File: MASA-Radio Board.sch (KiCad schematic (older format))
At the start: 50 parts, among them IC1 FAN4010IL6X_F113, IC2 FAN4010IL6X_F113, J1 Conn_01x02, J2 Conn_01x02_Male, J3 Conn_01x02_Male, J4 Conn_01x03_Male, J5 Conn_01x06, J6 SC_19-20, J7 Conn_01x06, J8 Conn_01x02, J9 UJ2-MBH-1-SMT-TR, U1 MP5077GG-Z, U2 BL654PA, U3 MIC5504-3.3YM5, U4 MP5077GG-Z

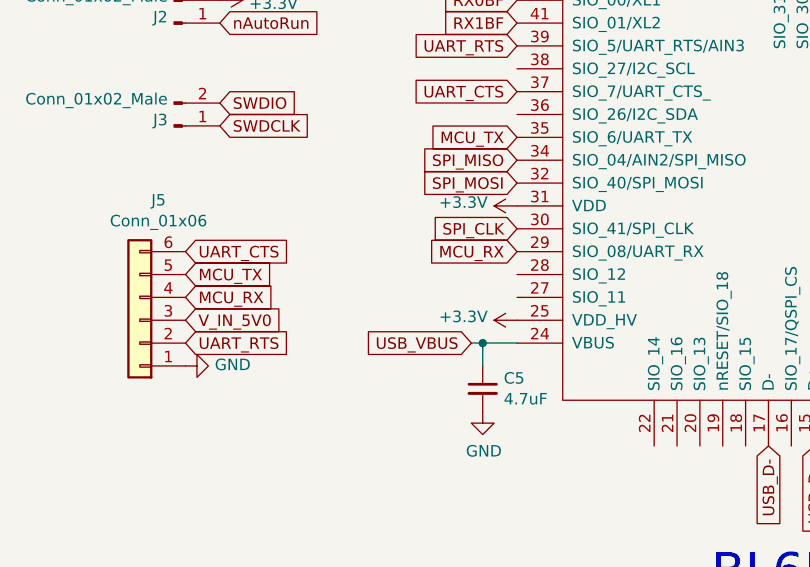
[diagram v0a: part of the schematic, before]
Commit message: Added caps on 3.3V MCU
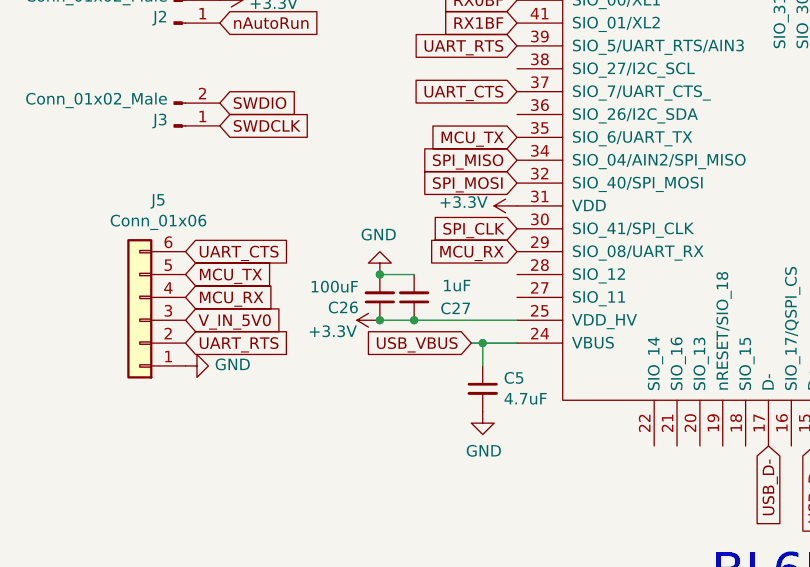
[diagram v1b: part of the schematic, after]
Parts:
- added C26: 100uF, Capacitor_SMD:C_0603_1608Metric, symbol Device:C_Small
- added C27: 1uF, Capacitor_SMD:C_0603_1608Metric, symbol Device:C_Small
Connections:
- wire segments 94 -> 97
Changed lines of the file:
@@
 L power:+3.3V #PWR010
 U 1 1 5E17DA05
-P 11450 4400
-F 0 "#PWR010" H 11450 4250 50  0001 C CNN
-F 1 "+3.3V" V 11465 4528 50  0000 L CNN
-F 2 "" H 11450 4400 50  0001 C CNN
-F 3 "" H 11450 4400 50  0001 C CNN
-	1    11450 4400
+P 10850 4400
+F 0 "#PWR010" H 10850 4250 50  0001 C CNN
+F 1 "+3.3V" V 10800 4500 50  0000 L CNN
+F 2 "" H 10850 4400 50  0001 C CNN
+F 3 "" H 10850 4400 50  0001 C CNN
+	1    10850 4400
 	0    -1   -1   0
 $EndComp
@@
 Text GLabel 11250 4500 0    50   Input ~ 0
 USB_VBUS
-$Comp
-L power:GND #PWR014
-U 1 1 5E19D471
-P 11300 4800
-F 0 "#PWR014" H 11300 4550 50  0001 C CNN
-F 1 "GND" H 11305 4627 50  0000 C CNN
-F 2 "" H 11300 4800 50  0001 C CNN
-F 3 "" H 11300 4800 50  0001 C CNN
-	1    11300 4800
-	1    0    0    -1
-$EndComp
-$Comp
-L Device:C_Small C5
-U 1 1 5E19C8DE
-P 11300 4700
-F 0 "C5" H 11392 4746 50  0000 L CNN
-F 1 "4.7uF" H 11392 4655 50  0000 L CNN
-F 2 "Capacitor_SMD:C_0603_1608Metric" H 11300 4700 50  0001 C CNN
-F 3 "~" H 11300 4700 50  0001 C CNN
-	1    11300 4700
-	1    0    0    -1
-$EndComp
 Connection ~ 11300 4500
 Text GLabel 11850 8400 0    50   Input ~ 0
@@
 	1    0    0    1
 $EndComp
-$Comp
-L MASA_Library:BL654PA U2
-U 1 1 5E18798E
-P 13150 3750
-F 0 "U2" H 14894 3796 50  0000 L CNN
-F 1 "BL654PA" H 14894 3705 50  0000 L CNN
-F 2 "MASA_Library:BL654PA" H 13150 3750 50  0001 C CNN
-F 3 "" H 13150 3750 50  0001 C CNN
-	1    13150 3750
-	1    0    0    -1
-$EndComp
 Text Notes 12300 13000 0    157  ~ 0
 Temperature Sensor
-Wire Wire Line
-	11300 4500 11450 4500
 Text Notes 15500 2850 0    50   ~ 0
 Reserve I/O Pins for:
@@
 Text GLabel 12900 2550 1    50   Input ~ 0
 TSENSE
+Wire Wire Line
+	11300 4500 11450 4500
+$Comp
+L MASA_Library:BL654PA U2
+U 1 1 5E18798E
+P 13150 3750
+F 0 "U2" H 14894 3796 50  0000 L CNN
+F 1 "BL654PA" H 14894 3705 50  0000 L CNN
+F 2 "MASA_Library:BL654PA" H 13150 3750 50  0001 C CNN
+F 3 "" H 13150 3750 50  0001 C CNN
+	1    13150 3750
+	1    0    0    -1
+$EndComp
+$Comp
+L Device:C_Small C5
+U 1 1 5E19C8DE
+P 11300 4700
+F 0 "C5" H 11392 4746 50  0000 L CNN
+F 1 "4.7uF" H 11392 4655 50  0000 L CNN
+F 2 "Capacitor_SMD:C_0603_1608Metric" H 11300 4700 50  0001 C CNN
+F 3 "~" H 11300 4700 50  0001 C CNN
+	1    11300 4700
+	1    0    0    -1
+$EndComp
+$Comp
+L power:GND #PWR014
+U 1 1 5E19D471
+P 11300 4800
+F 0 "#PWR014" H 11300 4550 50  0001 C CNN
+F 1 "GND" H 11305 4627 50  0000 C CNN
+F 2 "" H 11300 4800 50  0001 C CNN
+F 3 "" H 11300 4800 50  0001 C CNN
+	1    11300 4800
+	1    0    0    -1
+$EndComp
+$Comp
+L Device:C_Small C27
+U 1 1 5E84D23C
+P 11000 4300
+F 0 "C27" H 10750 4350 50  0000 L CNN
+F 1 "1uF" H 10750 4250 50  0000 L CNN
+F 2 "Capacitor_SMD:C_0603_1608Metric" H 11000 4300 50  0001 C CNN
+F 3 "~" H 11000 4300 50  0001 C CNN
+	1    11000 4300
+	-1   0    0    1
+$EndComp
+$Comp
+L Device:C_Small C26
+U 1 1 5E84FF5A
+P 10850 4300
+F 0 "C26" H 10942 4346 50  0000 L CNN
+F 1 "100uF" H 10942 4255 50  0000 L CNN
+F 2 "Capacitor_SMD:C_0603_1608Metric" H 10850 4300 50  0001 C CNN
+F 3 "~" H 10850 4300 50  0001 C CNN
+	1    10850 4300
+	-1   0    0    1
+$EndComp
+$Comp
+L power:GND #PWR073
+U 1 1 5E84FF60
+P 10850 4200
+F 0 "#PWR073" H 10850 3950 50  0001 C CNN
+F 1 "GND" H 10855 4027 50  0000 C CNN
+F 2 "" H 10850 4200 50  0001 C CNN
+F 3 "" H 10850 4200 50  0001 C CNN
+	1    10850 4200
+	-1   0    0    1
+$EndComp
+Connection ~ 10850 4200
+Wire Wire Line
+	11000 4400 10850 4400
+Connection ~ 10850 4400
+Wire Wire Line
+	11000 4400 11450 4400
+Connection ~ 11000 4400
+Wire Wire Line
+	11000 4200 10850 4200
 $EndSCHEMATC

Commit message: Fixed caps and added grounding
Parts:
- C26: value 100uF -> 100nF
- C27: value 1uF -> 1nF
- MOD1: symbol dk_RF-Transceiver-Modules:XBP9B-DPST-001 -> MASA-Radio-Board-rescue:XBP9B-DPST-001-dk_RF-Transceiver-Modules
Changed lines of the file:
@@
 EESchema Schematic File Version 4
+LIBS:MASA-Radio Board-cache
 EELAYER 30 0
 EELAYER END
@@
 	4850 7650 4950 7650
 $Comp
-L dk_RF-Transceiver-Modules:XBP9B-DPST-001 MOD1
+L MASA-Radio-Board-rescue:XBP9B-DPST-001-dk_RF-Transceiver-Modules MOD1
 U 1 1 5E2D5997
 P 4950 8600
@@
 P 11000 4300
 F 0 "C27" H 10750 4350 50  0000 L CNN
-F 1 "1uF" H 10750 4250 50  0000 L CNN
+F 1 "1nF" H 10750 4250 50  0000 L CNN
 F 2 "Capacitor_SMD:C_0603_1608Metric" H 11000 4300 50  0001 C CNN
 F 3 "~" H 11000 4300 50  0001 C CNN
@@
 P 10850 4300
 F 0 "C26" H 10942 4346 50  0000 L CNN
-F 1 "100uF" H 10942 4255 50  0000 L CNN
+F 1 "100nF" H 10942 4255 50  0000 L CNN
 F 2 "Capacitor_SMD:C_0603_1608Metric" H 10850 4300 50  0001 C CNN
 F 3 "~" H 10850 4300 50  0001 C CNN

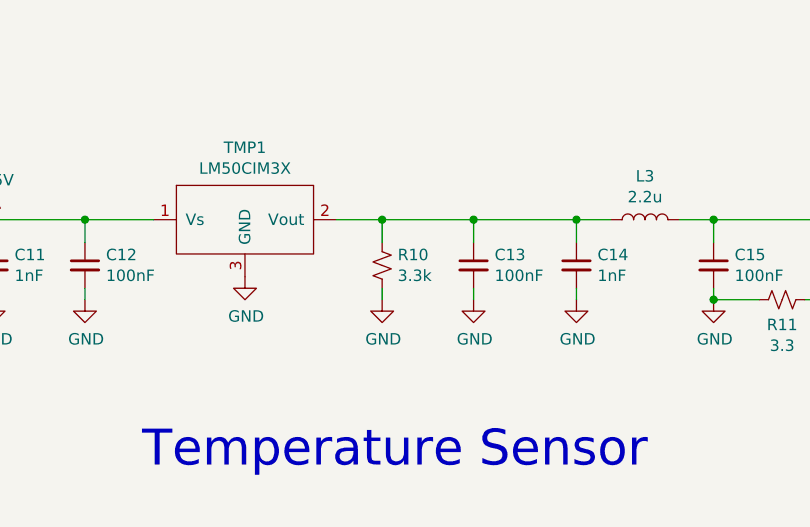
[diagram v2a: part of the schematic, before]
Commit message: Removed resistor from temp sensor
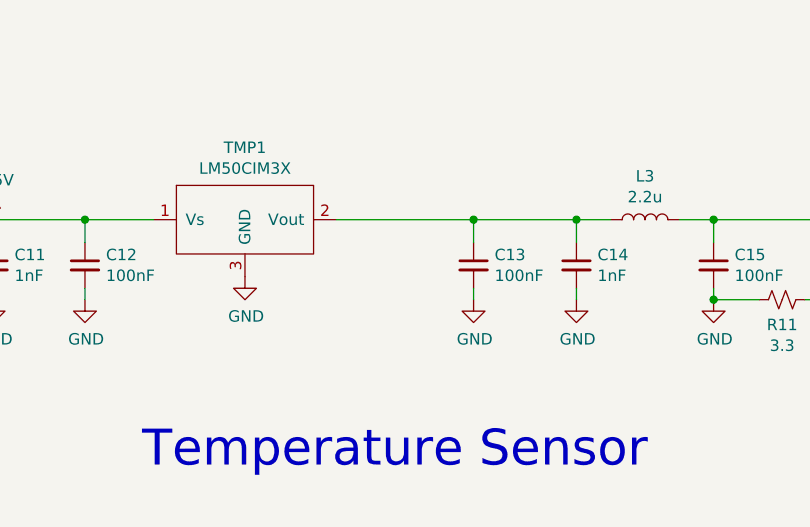
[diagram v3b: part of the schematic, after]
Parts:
- removed R10: 3.3k, Resistor_SMD:R_0603_1608Metric, symbol Device:R_Small_US
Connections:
- wire segments 97 -> 94
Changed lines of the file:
@@
 EELAYER 30 0
 EELAYER END
-$Descr A1 33110 23386
+$Descr A2 23386 16535
 encoding utf-8
 Sheet 1 2
@@
 	13750 11900 14200 11900
 Connection ~ 13750 11900
-Connection ~ 13350 11900
-Wire Wire Line
-	13350 11900 13750 11900
 Wire Wire Line
 	13750 12250 13750 12200
@@
 F 3 "~" H 13750 12100 50  0001 C CNN
 	1    13750 12100
-	1    0    0    -1
-$EndComp
-Wire Wire Line
-	13350 11900 13150 11900
-Wire Wire Line
-	13350 12000 13350 11900
-Wire Wire Line
-	13350 12250 13350 12200
-$Comp
-L power:GND #PWR043
-U 1 1 5E22C0FA
-P 13350 12250
-F 0 "#PWR043" H 13350 12000 50  0001 C CNN
-F 1 "GND" H 13355 12077 50  0000 C CNN
-F 2 "" H 13350 12250 50  0001 C CNN
-F 3 "" H 13350 12250 50  0001 C CNN
-	1    13350 12250
-	1    0    0    -1
-$EndComp
-$Comp
-L Device:R_Small_US R10
-U 1 1 5E22780B
-P 13350 12100
-F 0 "R10" H 13418 12146 50  0000 L CNN
-F 1 "3.3k" H 13418 12055 50  0000 L CNN
-F 2 "Resistor_SMD:R_0603_1608Metric" H 13350 12100 50  0001 C CNN
-F 3 "~" H 13350 12100 50  0001 C CNN
-	1    13350 12100
 	1    0    0    -1
 $EndComp
@@
 Wire Wire Line
 	11000 4200 10850 4200
+Wire Wire Line
+	13150 11900 13750 11900
 $EndSCHEMATC

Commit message: Added filters and connected missing analog lines. Also fixed USB
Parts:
- removed C1, C9: 10nF, Capacitor_SMD:C_0402_1005Metric, symbol Device:C_Small
- removed C10: 22nF, Capacitor_SMD:C_0603_1608Metric, symbol Device:C_Small
- removed C11, C14, C27: 1nF, Capacitor_SMD:C_0603_1608Metric, symbol Device:C_Small
- removed C12, C13, C15, C26: 100nF, Capacitor_SMD:C_0603_1608Metric, symbol Device:C_Small
- removed C16: 2.2uF, Capacitor_SMD:C_0603_1608Metric, symbol Device:C_Small
- removed C17, C4, C6, C8: 1uF, Capacitor_SMD:C_0603_1608Metric, symbol Device:C_Small
- removed C2: 22uF, Capacitor_SMD:C_0603_1608Metric, symbol Device:C_Small
- removed C3: 0.68uF, Capacitor_SMD:C_0603_1608Metric, symbol Device:C_Small
- removed C5: 4.7uF, Capacitor_SMD:C_0603_1608Metric, symbol Device:C_Small
- removed C7: 47pF, Capacitor_SMD:C_0603_1608Metric, symbol Device:C_Small
- removed D1, D2: D_TVS, Diode_SMD:D_SOD-523, symbol Device:D_TVS
- removed IC1, IC2: FAN4010IL6X_F113, MASA_Library:6-LEAD_MICROPAK, symbol FAN4010IL6X_F113:FAN4010IL6X_F113
- removed J1, J8: Conn_01x02, Jumper:SolderJumper-2_P1.3mm_Open_TrianglePad1.0x1.5mm, symbol Connector_Generic:Conn_01x02
- removed J2, J3: Conn_01x02_Male, Connector_PinHeader_2.54mm:PinHeader_1x02_P2.54mm_Vertical, symbol Connector:Conn_01x02_Male
- removed J4: Conn_01x03_Male, Connector_PinHeader_2.54mm:PinHeader_1x03_P2.54mm_Vertical, symbol Connector:Conn_01x03_Male
- removed J5, J7: Conn_01x06, Connector_PinHeader_2.54mm:PinHeader_1x06_P2.54mm_Vertical, symbol Connector_Generic:Conn_01x06
- removed J6: SC_19-20, MASA_Library:Stack_Connector_2019_2020, symbol MASA_Library:SC_19-20
- removed J9: UJ2-MBH-1-SMT-TR, digikey-footprints:USB_Mini_B_Female_UJ2-MBH-1-SMT-TR, symbol MASA-Radio-Board-rescue:UJ2-MBH-1-SMT-TR-dk_USB-DVI-HDMI-Connectors
- removed L1, L2: 4.7uH, Inductor_SMD:L_0603_1608Metric, symbol Device:L
- removed L3: 2.2u, Inductor_SMD:L_0603_1608Metric, symbol Device:L
- removed MOD1: XBP9B-DPST-001, digikey-footprints:XBEE_PRO-20_THT, symbol MASA-Radio-Board-rescue:XBP9B-DPST-001-dk_RF-Transceiver-Modules
- removed R1: 1, Resistor_SMD:R_0603_1608Metric, symbol Device:R_US
- removed R11: 3.3, Resistor_SMD:R_0603_1608Metric, symbol Device:R_Small_US
- removed R2: 200k, Resistor_SMD:R_0603_1608Metric, symbol Device:R_US
- removed R3: 200m, Resistor_SMD:R_0603_1608Metric, symbol Device:R_US
- removed R4: 3k, Resistor_SMD:R_0603_1608Metric, symbol Device:R_US
- removed R5: 100k, Resistor_SMD:R_0603_1608Metric, symbol Device:R_Small_US
- removed R6: 1, Resistor_SMD:R_0402_1005Metric, symbol Device:R_US
- removed R7: 1, Resistor_SMD:R_0603_1608Metric, symbol Device:R_Small_US
- removed R8: 3k, Resistor_SMD:R_0603_1608Metric, symbol Device:R_Small_US
- removed R9: 820k, Resistor_SMD:R_0603_1608Metric, symbol Device:R_Small_US
- removed TMP1: LM50CIM3X, Package_TO_SOT_SMD:SOT-23, symbol MASA_Library:LM50CIM3X
- removed U1, U4: MP5077GG-Z, MASA_Library:MP5077GG-Z, symbol MASA_Library:MP5077GG-Z
- removed U2: BL654PA, MASA_Library:BL654PA, symbol MASA_Library:BL654PA
- removed U3: MIC5504-3.3YM5, Package_TO_SOT_SMD:SOT-23-5, symbol Regulator_Linear:MIC5504-3.3YM5
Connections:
- net labels removed: +3.3V, +5V, 3V3, 3V3Sense, 5V0, CAN_H, CAN_INT, CAN_L, CAN_RST, CS, GND, MCU_RX, MCU_TX, RX0BF, RX1BF, SPI_CLK, SPI_MISO, SPI_MOSI, STACK_3.3V, SWDCLK, SWDIO, TSENSE, TX0RTS, TX1RTS, TX2RTS, UART_CTS, UART_RTS, USB_D+, USB_D-, USB_VBUS, V_IN_5V0, XBee_RX, XBee_TX, nAutoRun
- wire segments 94 -> 0
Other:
- note removed: "-CS*\n-SCK\n-CAN_INT\n-RX0BF*\n-RX1BF*\n-TXORTS*\n-TX1RTS*\n-TX2RTS*\n-CAN_RESET*\n\n-TSENSE"
- note removed: "5V Power Conditioning"
- note removed: "BL654PA MCU"
- note removed: "CAN_Template"
- note removed: "Current Sense IC"
- note removed: "Linear Voltage Regulator IC"
- note removed: "Linear Voltage Regulator IC 1 Output 300mA SOT-23-5"
- note removed: "Load Switch"
- note removed: "Reserve I/O Pins for:"
- note removed: "Stack Connector"
- note removed: "Temperature Sensor"
- note removed: "USB"
- note removed: "XBee"

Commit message: Unbroke schematic
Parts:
- added C1, C9: 10nF, Capacitor_SMD:C_0402_1005Metric, symbol Device:C_Small
- added C10: 22nF, Capacitor_SMD:C_0603_1608Metric, symbol Device:C_Small
- added C11, C14, C27: 1nF, Capacitor_SMD:C_0603_1608Metric, symbol Device:C_Small
- added C12, C13, C15, C26: 100nF, Capacitor_SMD:C_0603_1608Metric, symbol Device:C_Small
- added C16: 2.2uF, Capacitor_SMD:C_0603_1608Metric, symbol Device:C_Small
- added C17, C3: 47nF, Capacitor_SMD:C_0603_1608Metric, symbol Device:C_Small
- added C2: 22uF, Capacitor_SMD:C_0603_1608Metric, symbol Device:C_Small
- added C28, C32: 1nF, Capacitor_SMD:C_0402_1005Metric, symbol Device:C_Small
- added C33: 2.2pF, Capacitor_SMD:C_0603_1608Metric, symbol Device:C_Small
- added C34: 470pF, Capacitor_SMD:C_0603_1608Metric, symbol Device:C_Small
- added C4, C6, C8: 1uF, Capacitor_SMD:C_0603_1608Metric, symbol Device:C_Small
- added C5: 4.7uF, Capacitor_SMD:C_0603_1608Metric, symbol Device:C_Small
- added C7: 47pF, Capacitor_SMD:C_0603_1608Metric, symbol Device:C_Small
- added D1, D2: D_TVS, Diode_SMD:D_SOD-523, symbol Device:D_TVS
- added IC1, IC2: FAN4010IL6X_F113, MASA_Library:6-LEAD_MICROPAK, symbol FAN4010IL6X_F113:FAN4010IL6X_F113
- added J1, J8: Conn_01x02, Jumper:SolderJumper-2_P1.3mm_Open_TrianglePad1.0x1.5mm, symbol Connector_Generic:Conn_01x02
- added J2, J3: Conn_01x02_Male, Connector_PinHeader_2.54mm:PinHeader_1x02_P2.54mm_Vertical, symbol Connector:Conn_01x02_Male
- added J4: Conn_01x03_Male, Connector_PinHeader_2.54mm:PinHeader_1x03_P2.54mm_Vertical, symbol Connector:Conn_01x03_Male
- added J5, J7: Conn_01x06, Connector_PinHeader_2.54mm:PinHeader_1x06_P2.54mm_Vertical, symbol Connector_Generic:Conn_01x06
- added J6: SC_19-20, MASA_Library:Stack_Connector_2019_2020, symbol MASA_Library:SC_19-20
- added J9: UJ2-MBH-1-SMT-TR, digikey-footprints:USB_Mini_B_Female_UJ2-MBH-1-SMT-TR, symbol dk_USB-DVI-HDMI-Connectors:UJ2-MBH-1-SMT-TR
- added L1, L2: 4.7uH, Inductor_SMD:L_0603_1608Metric, symbol Device:L
- added L3: 2.2u, Inductor_SMD:L_0603_1608Metric, symbol Device:L
- added MOD1: XBP9B-DPST-001, digikey-footprints:XBEE_PRO-20_THT, symbol MASA-Radio-Board-rescue:XBP9B-DPST-001-dk_RF-Transceiver-Modules
- added R1: 1, Resistor_SMD:R_0603_1608Metric, symbol Device:R_US
- added R10, R16: 1k, Resistor_SMD:R_0402_1005Metric, symbol Device:R_US
- added R11: 3.3, Resistor_SMD:R_0603_1608Metric, symbol Device:R_Small_US
- added R18: 470, Resistor_SMD:R_0603_1608Metric, symbol Device:R_US
- added R2: 200k, Resistor_SMD:R_0603_1608Metric, symbol Device:R_US
- added R3: 200m, Resistor_SMD:R_0603_1608Metric, symbol Device:R_US
- added R4: 3k, Resistor_SMD:R_0603_1608Metric, symbol Device:R_US
- added R5: 100k, Resistor_SMD:R_0603_1608Metric, symbol Device:R_Small_US
- added R6: 1, Resistor_SMD:R_0402_1005Metric, symbol Device:R_US
- added R7: 1, Resistor_SMD:R_0603_1608Metric, symbol Device:R_Small_US
- added R8: 3k, Resistor_SMD:R_0603_1608Metric, symbol Device:R_Small_US
- added R9: 820k, Resistor_SMD:R_0603_1608Metric, symbol Device:R_Small_US
- added TMP1: LM50CIM3X, Package_TO_SOT_SMD:SOT-23, symbol MASA_Library:LM50CIM3X
- added U1, U4: MP5077GG-Z, MASA_Library:MP5077GG-Z, symbol MASA_Library:MP5077GG-Z
- added U2: BL654PA, MASA_Library:BL654PA, symbol MASA_Library:BL654PA
- added U3: MIC5504-3.3YM5, Package_TO_SOT_SMD:SOT-23-5, symbol Regulator_Linear:MIC5504-3.3YM5
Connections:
- new net: C4.2, J4.3 (Pin_3), U3.5 (VOUT)
- new net: J6.25 (UART1_TX), R5.1
- new net: C34.2, J6.27 (UART1_RX), R18.1
- new net: IC1.1 (VIN), J4.2 (Pin_2), R3.2
- new net: C1.2, R1.2
- new net: C2.1, D1.2 (A2), J1.1 (Pin_1), L1.1, U1.10 (Vout), U1.7 (Vout), U1.8 (Vout), U1.9 (Vout)
- new net: R2.2, U1.4 (Ilim)
- new net: C3.1, U1.5 (SS)
- new net: C28.1, R10.2, U2.45 (SIO_30/AIN6)
- new net: C32.2, R16.2, U2.49 (SIO_03/AIN1)
- new net: C13.1, C14.1, L3.1, TMP1.2 (Vout)
- new net: C16.2, R11.2
- new net: C10.1, IC2.1 (VIN), L2.2, R7.1
- new net: C9.1, D2.2 (A2), J8.1 (Pin_1), L2.1, U4.10 (Vout), U4.7 (Vout), U4.8 (Vout), U4.9 (Vout)
- new net: R9.2, U4.4 (Ilim)
- new net: C17.1, U4.5 (SS)
- new net: C10.2, R6.2
- new net +3V3: C26.1, C27.1, C7.2, C8.2, IC1.6 (LOAD), J2.2 (Pin_2), MOD1.1 (Vcc), R3.1, U2.25 (VDD_HV), U2.31 (VDD)
- new net +5V: C11.1, C12.1, IC2.6 (LOAD), R7.2, TMP1.1 (Vs)
- new net 3V3: J1.2 (Pin_2), J6.2 (3V3), J6.3 (3V3), J6.6 (3V3), J6.7 (3V3), U1.11 (Vin), U1.6 (Vin)
- new net 3V3Sense: IC1.3 (IOUT), R16.1, R4.1
- new net 5V0: J6.34 (5V0), J6.35 (5V0), J6.38 (5V0), J6.39 (5V0), J8.2 (Pin_2), U1.1 (EN), U1.3 (Vcc), U4.1 (EN), U4.11 (Vin), U4.3 (Vcc), U4.6 (Vin)
- new net 5VSense: IC2.3 (IOUT), R10.1, R8.1
- new net CAN_H: J6.21 (CAN_H)
- new net CAN_INT: U2.59 (NFC1/SIO_09)
- new net CAN_L: J6.23 (CAN_L)
- new net CAN_RST: U2.63 (SIO_38)
- new net CS: U2.61 (SIO_37)
- new net GND: C11.2, C12.2, C13.2, C14.2, C15.2, C17.2, C2.2, C26.2, C27.2, C28.2, C3.2, C32.1, C33.2, C34.1, C4.1, C5.2, C6.2, C7.1, C8.1, C9.2, D1.1 (A1), D2.1 (A1), IC1.5 (GND), IC2.5 (GND), J5.1 (Pin_1), J6.1 (GND), J6.19 (GND), J6.20 (GND), J6.36 (GND), J6.37 (GND), J6.4 (GND), J6.40 (GND), J6.5 (GND), J7.1 (Pin_1), J9.5, J9.SH, MOD1.10 (GND), MOD1.14 (VREF), R1.1, R11.1, R2.1, R4.2, R6.1, R8.2, R9.1, TMP1.3 (GND), U1.2 (GND), U2.0 (GND), U2.23 (GND), U2.26 (GND), U2.33 (GND), U2.40 (GND), U2.43 (GND), U2.47 (GND), U2.52 (GND), U2.55 (GND), U2.58 (GND), U2.65 (GND), U2.66 (GND), U2.67 (GND), U2.68 (GND), U2.69 (GND), U2.70 (GND), U2.71 (GND), U2.72 (GND), U2.73 (GND), U2.74 (GND), U2.75 (GND), U2.76 (GND), U2.77 (GND), U2.78 (GND), U2.79 (GND), U3.2 (GND), U4.2 (GND)
- new net MCU_RX: J5.4 (Pin_4), U2.29 (SIO_08/UART_RX)
- new net MCU_TX: J5.5 (Pin_5), U2.35 (SIO_6/UART_TX)
- new net RX0BF: U2.42 (SIO_00/XL1)
- new net RX1BF: U2.41 (SIO_01/XL2)
- new net SPI_CLK: U2.30 (SIO_41/SPI_CLK)
- new net SPI_MISO: U2.34 (SIO_04/AIN2/SPI_MISO)
- new net SPI_MOSI: U2.32 (SIO_40/SPI_MOSI)
- new net STACK_3.3V: C1.1, J4.1 (Pin_1), L1.2
- new net SWDCLK: J3.1 (Pin_1), U2.3 (SWDCLK)
- new net SWDIO: J3.2 (Pin_2), U2.1 (SWDIO)
- new net TSENSE: C15.1, C16.1, L3.2, U2.48 (SIO_29/AIN5)
- new net TX0RTS: U2.57 (NFC2/SIO_10)
- new net TX1RTS: U2.53 (SIO_47)
- new net TX2RTS: U2.56 (SIO_45)
- new net UART_CTS: J5.6 (Pin_6), U2.37 (SIO_7/UART_CTS_)
- new net UART_RTS: J5.2 (Pin_2), U2.39 (SIO_5/UART_RTS/AIN3)
- new net USB_D+: J9.3, U2.15 (D+)
- new net USB_D-: J9.2, U2.17 (D-)
- new net USB_VBUS: C5.1, J9.1, U2.24 (VBUS)
- new net V_IN_5V0: C6.1, J5.3 (Pin_3), J7.3 (Pin_3), U3.1 (VIN), U3.3 (EN)
- new net XBee_RX: C33.1, J7.4 (Pin_4), MOD1.3 (UART/DIN/Config), R5.2
- new net XBee_TX: J7.5 (Pin_5), MOD1.2 (UART/DOUT), R18.2
- new net nAutoRun: J2.1 (Pin_1), U2.5 (SIO_35/nAutoRUN)
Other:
- note added: "-CS*\n-SCK\n-CAN_INT\n-RX0BF*\n-RX1BF*\n-TXORTS*\n-TX1RTS*\n-TX2RTS*\n-CAN_RESET*\n\n-TSENSE"
- note added: "5V Power Conditioning"
- note added: "BL654PA MCU"
- note added: "CAN_Template"
- note added: "Current Sense IC"
- note added: "Linear Voltage Regulator IC"
- note added: "Linear Voltage Regulator IC 1 Output 300mA SOT-23-5"
- note added: "Load Switch"
- note added: "Reserve I/O Pins for:"
- note added: "Stack Connector"
- note added: "Temperature Sensor"
- note added: "USB"
- note added: "XBee"
